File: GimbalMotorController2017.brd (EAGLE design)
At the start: 112.4 x 80 mm, 143 parts, among them J3 APP_2POS_CONFIG5V_HORIZ, Q1 MOSFET-NCHANNELFQP30N06L, Q2 MOSFET-NCHANNELFQP30N06L, Q3 MOSFET-NCHANNELFQP30N06L, Q4 MOSFET-NCHANNELFQP30N06L, Q5 MOSFET-NCHANNELFQP30N06L, Q6 MOSFET-NCHANNELFQP30N06L, Q7 MOSFET-PCHANNEL, Q8 MOSFET-PCHANNEL, Q9 MOSFET-NCHANNELAO3404A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

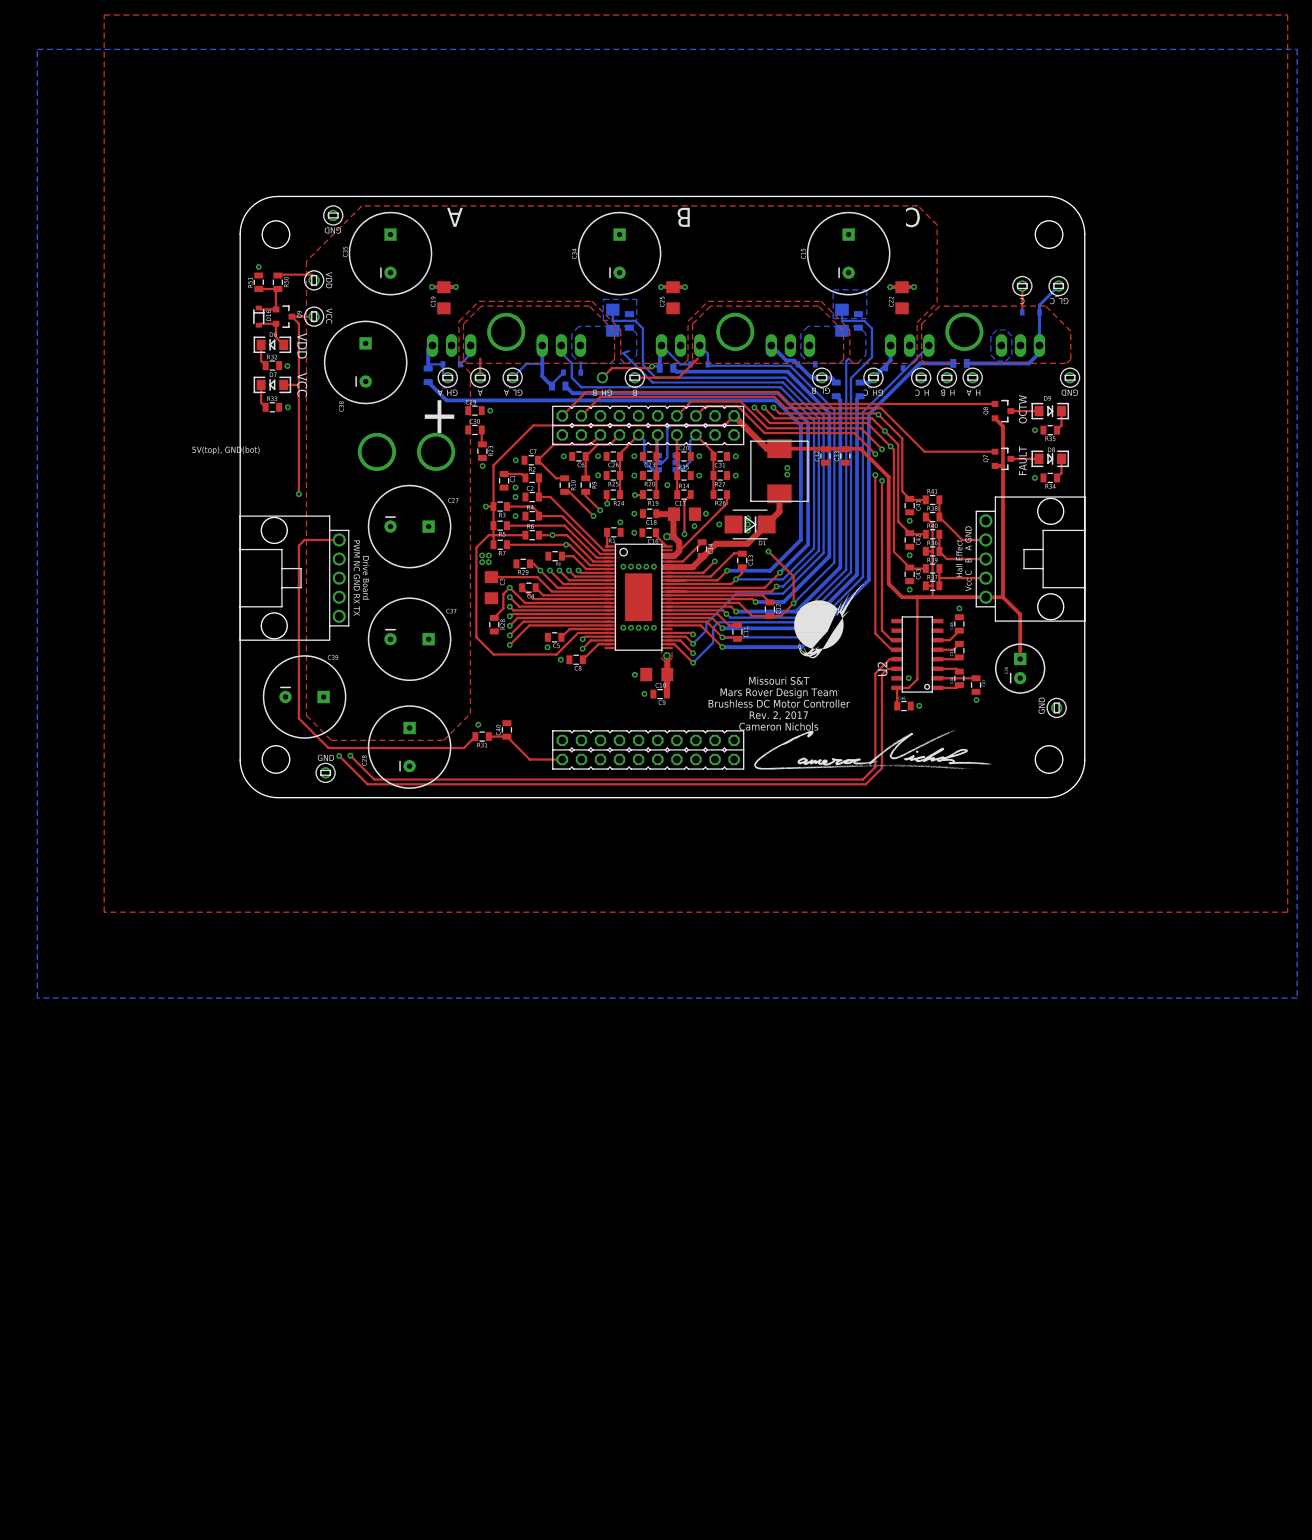
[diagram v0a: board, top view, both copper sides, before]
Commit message: changed power filtering cap count and R26 value for 12v to 3.3v conversion
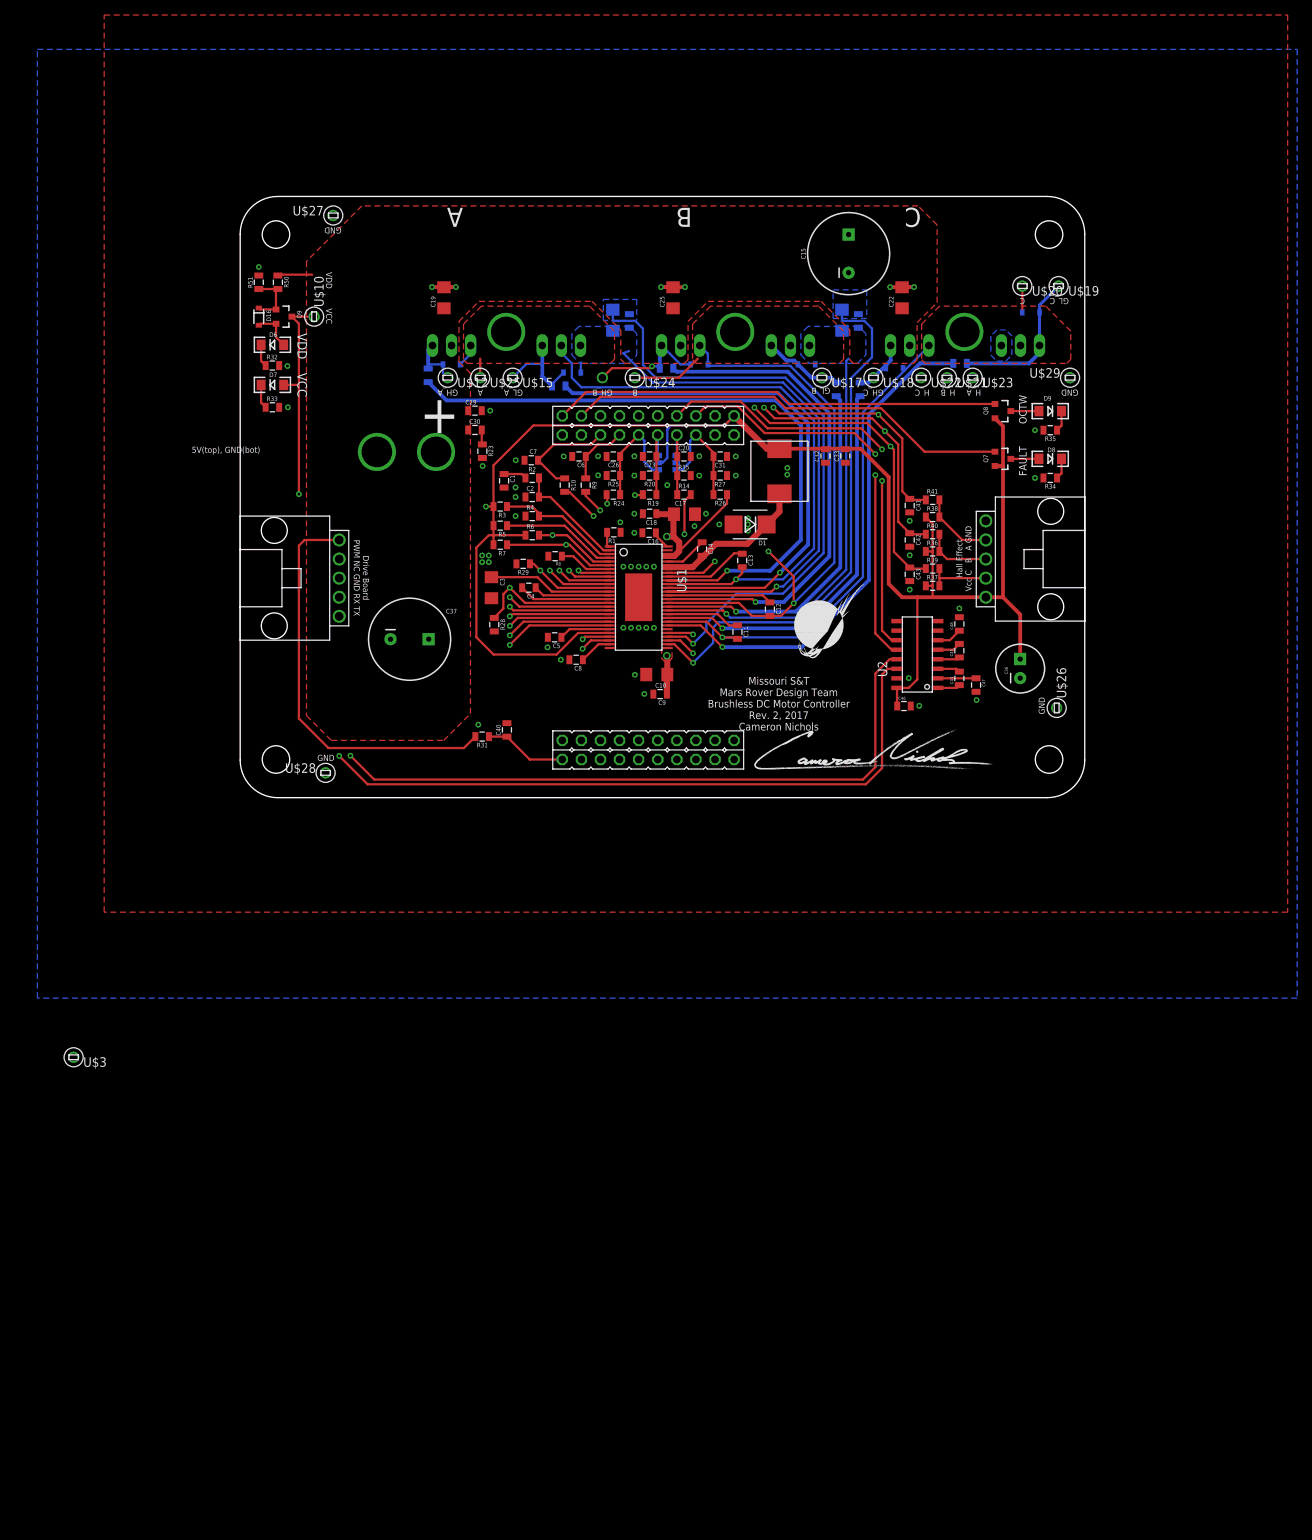
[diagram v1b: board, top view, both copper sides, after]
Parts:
- removed C27, C28, C34, C35, C38, C39: 220u, SparkFun-Passives:CPOL-RADIAL-1000UF-25V
- removed U$11: TEST_POINT_0.1INDIAM, MRDT-Connectors:TEST_POINT_0.1INDIAM
- added U$3: TEST_POINT_0.1INDIAM, MRDT-Connectors:TEST_POINT_0.1INDIAM
- R26: value 46.4k -> 13.2k
- U$1: device DRV8301:DCA -> MRDT-ICs:TFSOP-56
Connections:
- new net N$36: C15.1
- new net N$37: U$3.P$1
- net GND: no longer C27.2, C28.2, C34.2, C35.2, C38.2, C39.2
- net PVDD: no longer C15.1, C27.1, C28.1, C34.1, C35.1, C38.1, C39.1, U$11.P$1

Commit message: added CSD18533Q5A fets to Phase C in place of previously used fets
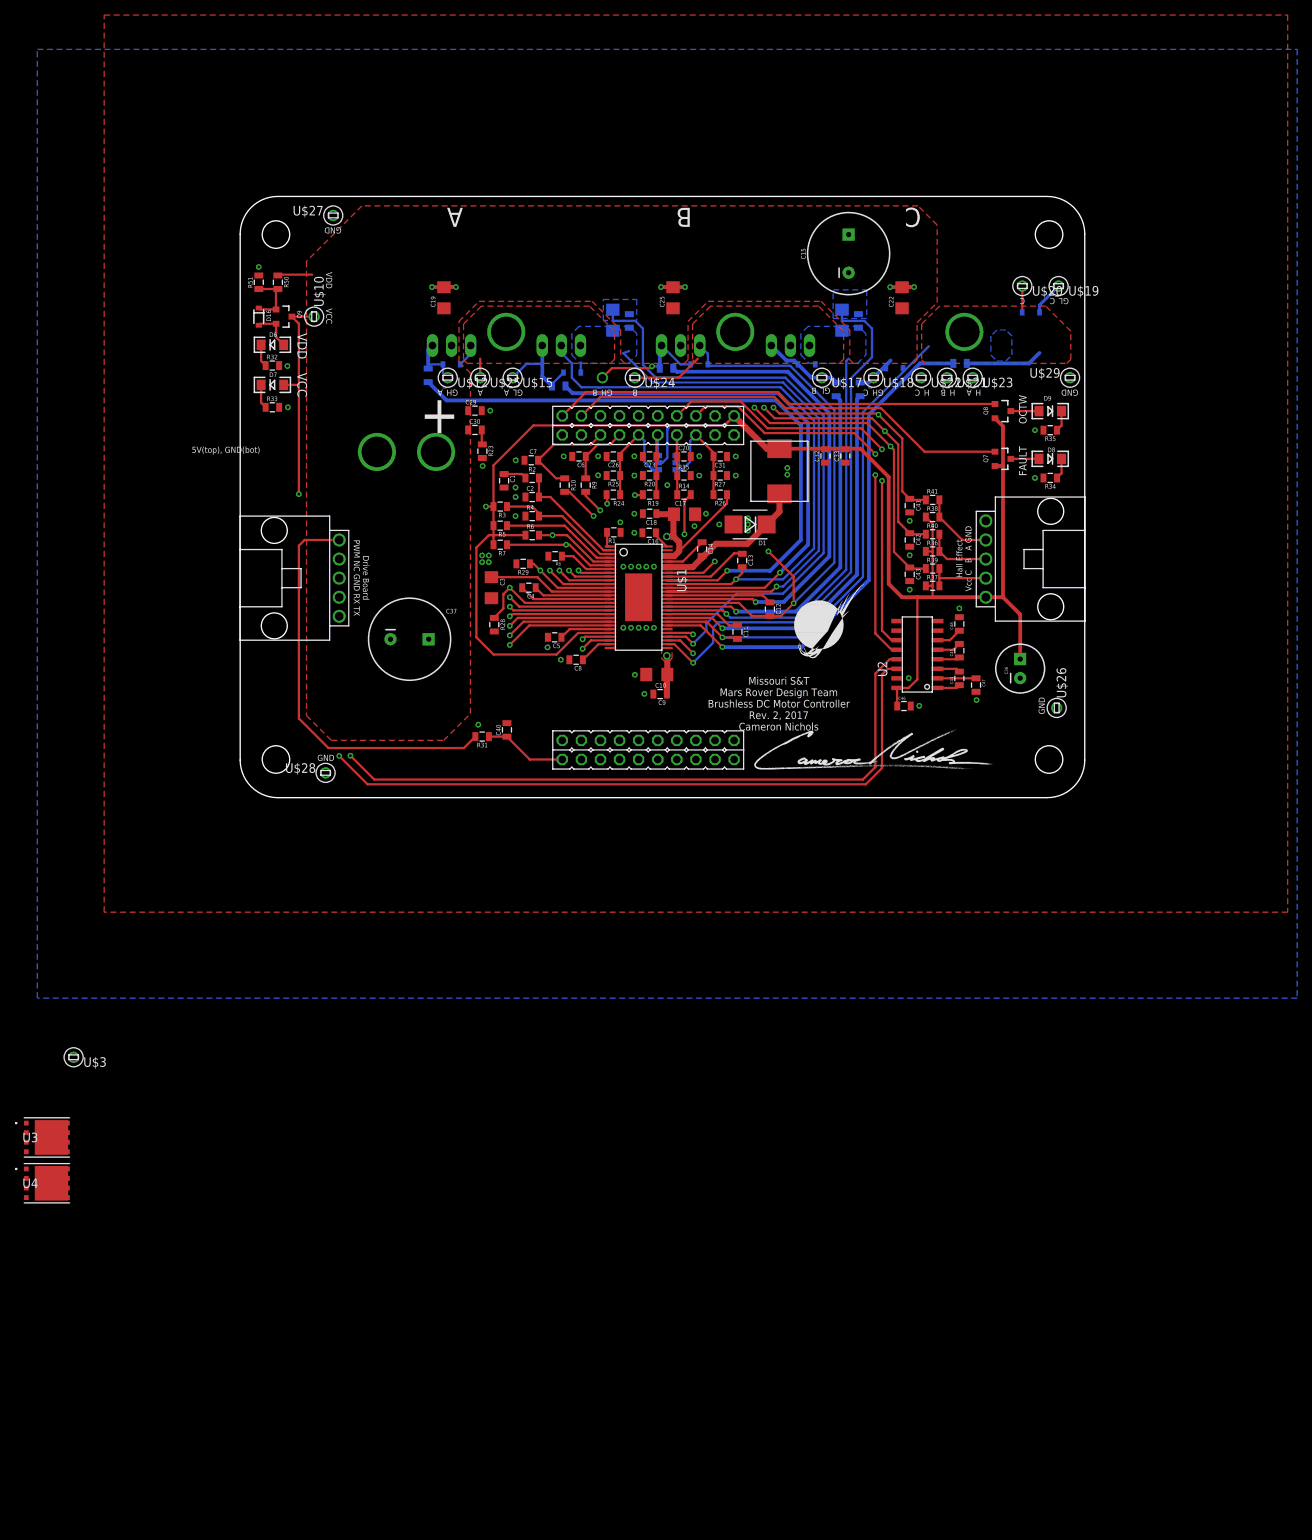
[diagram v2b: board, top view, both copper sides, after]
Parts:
- removed Q5, Q6: MOSFET-NCHANNELFQP30N06L, SparkFun-DiscreteSemi:TO220V
- added U3, U4: CSD18533Q5A, CSD18533:DQJ8
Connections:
- net GND: now also U4.3; no longer Q6.3
- net N$17: now also U3.4; no longer Q5.1
- net N$18: now also U4.4; no longer Q6.1
- net PVDD: now also U3.8; no longer Q5.2
- net SH_C: now also U3.3, U4.8; no longer Q5.3, Q6.2
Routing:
- net N$18: track 20.2 -> 14.8 mm
- net N$17: track 7.59 -> 5.59 mm
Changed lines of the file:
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@@
 <attribute name="PROD_ID" value="TRANS-10060" x="70.993" y="58.89625" size="1.778" layer="28" rot="MR180" display="off"/>
-</element>
-<element name="Q5" library="SparkFun-DiscreteSemi" package="TO220V" value="MOSFET-NCHANNELFQP30N06L" x="86.868" y="58.89625" smashed="yes" rot="MR180">
-<attribute name="NAME" x="90.424" y="55.46725" size="0.6096" layer="26" ratio="10" rot="MR180"/>
-<attribute name="PROD_ID" value="TRANS-10060" x="86.868" y="58.89625" size="1.778" layer="28" rot="MR180" display="off"/>
-</element>
-<element name="Q6" library="SparkFun-DiscreteSemi" package="TO220V" value="MOSFET-NCHANNELFQP30N06L" x="101.6" y="58.89625" smashed="yes" rot="MR0">
-<attribute name="NAME" x="98.171" y="61.05525" size="0.6096" layer="26" ratio="10" rot="MR0"/>
-<attribute name="PROD_ID" value="TRANS-10060" x="101.6" y="58.89625" size="1.778" layer="28" rot="MR0" display="off"/>
 </element>
 <element name="Q7" library="SparkFun-DiscreteSemi" package="SOT23-3" value="MOSFET-PCHANNEL" x="99.21875" y="43.815" smashed="yes" rot="R270">
@@
 <element name="C48" library="SparkFun-Passives" package="0805" value="0.1u" x="93.472" y="21.844" rot="R90"/>
 <element name="U$3" library="MRDT-Connectors" package="TEST_POINT_0.1INDIAM" value="TEST_POINT_0.1INDIAM" x="-24.384" y="-35.814"/>
+<element name="U3" library="CSD18533" package="DQJ8" value="CSD18533Q5A" x="-27.94" y="-46.482">
+<attribute name="MANUFACTURER_PART_NUMBER" value="CSD18533Q5A" x="-27.94" y="-46.482" size="1.778" layer="27" display="off"/>
+<attribute name="VENDOR" value="Texas Instruments" x="-27.94" y="-46.482" size="1.778" layer="27" display="off"/>
+</element>
+<element name="U4" library="CSD18533" package="DQJ8" value="CSD18533Q5A" x="-27.94" y="-52.578">
+<attribute name="MANUFACTURER_PART_NUMBER" value="CSD18533Q5A" x="-27.94" y="-52.578" size="1.778" layer="27" display="off"/>
+<attribute name="VENDOR" value="Texas Instruments" x="-27.94" y="-52.578" size="1.778" layer="27" display="off"/>
+</element>
 </elements>
 <signals>
@@
 </polygon>
 <contactref element="U$8" pad="5"/>
-<contactref element="Q6" pad="3"/>
 <polygon width="0.508" layer="16" thermals="no">
 <vertex x="97.663" y="60.16625"/>
@@
 <vertex x="-24.892" y="-19.558"/>
 </polygon>
-<wire x1="99.06" y1="58.89625" x2="101.847" y2="63.3095" width="0" layer="19" extent="16-16"/>
-<wire x1="108.204" y1="54.61" x2="99.06" y2="58.89625" width="0" layer="19" extent="1-1"/>
+<contactref element="U4" pad="3"/>
+<wire x1="108.204" y1="54.61" x2="101.847" y2="63.3095" width="0" layer="19" extent="16-16"/>
 <wire x1="104.66875" y1="47.625" x2="108.204" y2="54.61" width="0" layer="19" extent="1-1"/>
 <wire x1="103.53675" y1="47.625" x2="104.66875" y2="47.625" width="0" layer="19" extent="1-1"/>
@@
 <wire x1="17.78" y1="19.812" x2="31.59125" y2="20.84875" width="0" layer="19" extent="1-1"/>
 <wire x1="10.95375" y1="27.94" x2="17.78" y2="19.812" width="0" layer="19" extent="1-1"/>
-<wire x1="87.4395" y1="66.675" x2="99.06" y2="58.89625" width="0" layer="19" extent="1-1"/>
-<wire x1="80.04175" y1="63.0665" x2="84.2645" y2="66.675" width="0" layer="19" extent="16-16"/>
-<wire x1="77.851" y1="63.66175" x2="80.04175" y2="63.0665" width="0" layer="19" extent="16-16"/>
-<wire x1="78.74" y1="68.58" x2="77.851" y2="63.66175" width="0" layer="19" extent="16-16"/>
 <wire x1="15.97025" y1="44.73575" x2="30.00375" y2="43.931" width="0" layer="19" extent="1-1"/>
 <wire x1="4.1275" y1="50.673" x2="15.97025" y2="44.73575" width="0" layer="19" extent="1-1"/>
@@
 <wire x1="0.254" y1="69.342" x2="0.254" y2="68.21" width="0" layer="19" extent="1-1"/>
 <wire x1="10.16" y1="76.2" x2="0.254" y2="69.342" width="0" layer="19" extent="1-1"/>
+<wire x1="87.4395" y1="66.675" x2="101.847" y2="63.3095" width="0" layer="19" extent="16-16"/>
+<wire x1="80.04175" y1="63.0665" x2="84.2645" y2="66.675" width="0" layer="19" extent="16-16"/>
+<wire x1="77.851" y1="63.66175" x2="80.04175" y2="63.0665" width="0" layer="19" extent="16-16"/>
+<wire x1="78.74" y1="68.58" x2="77.851" y2="63.66175" width="0" layer="19" extent="16-16"/>
 <wire x1="23.3045" y1="66.675" x2="10.16" y2="76.2" width="0" layer="19" extent="1-1"/>
 <wire x1="47.371" y1="62.47765" x2="46.5345" y2="44.1325" width="0" layer="19" extent="1-16"/>
@@
 <wire x1="53.7845" y1="66.675" x2="49.56175" y2="63.0665" width="0" layer="19" extent="16-16"/>
 <wire x1="9.144" y1="2.032" x2="17.78" y2="19.812" width="0" layer="19" extent="1-1"/>
+<wire x1="-30.675071875" y1="-53.213" x2="9.144" y2="2.032" width="0" layer="19" extent="1-1"/>
 </signal>
 <signal name="N$3">
@@
 <contactref element="Q3" pad="2"/>
 <contactref element="C22" pad="1"/>
-<contactref element="Q5" pad="2"/>
 <contactref element="C25" pad="1"/>
 <contactref element="C29" pad="1"/>
@@
 </polygon>
 <contactref element="C37" pad="1"/>
-<wire x1="86.868" y1="58.89625" x2="85.852" y2="63.84625" width="0" layer="19" extent="1-1"/>
+<contactref element="U3" pad="8"/>
 <wire x1="56.388" y1="58.89625" x2="85.852" y2="63.84625" width="0" layer="19" extent="1-1"/>
 <wire x1="55.372" y1="63.84625" x2="56.388" y2="58.89625" width="0" layer="19" extent="1-1"/>
@@
 <wire x1="7.366" y1="68.326" x2="24.892" y2="63.84625" width="0" layer="19" extent="1-1"/>
 <wire x1="22.86" y1="19.812" x2="23.84425" y2="44.73575" width="0" layer="19" extent="1-1"/>
+<wire x1="-25.204928125" y1="-44.577" x2="22.86" y2="19.812" width="0" layer="19" extent="1-1"/>
 </signal>
 <signal name="GL_C">
@@
 <contactref element="U$1" pad="36"/>
 <contactref element="C11" pad="2"/>
-<contactref element="Q5" pad="3"/>
-<contactref element="Q6" pad="2"/>
 <contactref element="R24" pad="1"/>
 <contactref element="U$7" pad="P$1"/>
@@
 <wire x1="80.645" y1="50.031" x2="86.2365" y2="55.6225" width="0.3048" layer="16"/>
 <wire x1="86.2365" y1="55.6225" x2="89.408" y2="58.794" width="0.3048" layer="16"/>
-<wire x1="89.408" y1="58.794" x2="89.408" y2="58.89625" width="0.3048" layer="16"/>
 <wire x1="85.986" y1="55.88" x2="85.986" y2="55.873" width="0.3048" layer="16"/>
 <wire x1="85.986" y1="55.873" x2="86.2365" y2="55.6225" width="0.3048" layer="16"/>
+<contactref element="U3" pad="3"/>
+<contactref element="U4" pad="8"/>
+<wire x1="94.13875" y1="60.706" x2="101.854" y2="63.754" width="0" layer="19" extent="1-1"/>
+<wire x1="89.408" y1="58.794" x2="94.13875" y2="60.706" width="0" layer="19" extent="16-16"/>
+<wire x1="-25.204928125" y1="-50.673" x2="55.88" y2="17.272" width="0" layer="19" extent="1-15"/>
+<wire x1="-30.675071875" y1="-47.117" x2="-25.204928125" y2="-50.673" width="0" layer="19" extent="1-1"/>
 </signal>
 <signal name="GH_C">
@@
 </signal>
 <signal name="N$17">
-<contactref element="Q5" pad="1"/>
 <contactref element="R21" pad="1"/>
 <contactref element="D14" pad="C"/>
@@
 <wire x1="82.042" y1="54.61" x2="83.566" y2="56.134" width="0.508" layer="16"/>
 <wire x1="83.566" y1="56.134" x2="84.328" y2="56.896" width="0.508" layer="16"/>
-<wire x1="84.328" y1="56.896" x2="84.328" y2="58.89625" width="0.508" layer="16"/>
 <wire x1="83.686" y1="55.88" x2="83.566" y2="56" width="0.4064" layer="16"/>
 <wire x1="83.566" y1="56" x2="83.566" y2="56.134" width="0.4064" layer="16"/>
+<contactref element="U3" pad="4"/>
+<wire x1="-30.675071875" y1="-48.387" x2="80.264" y2="53.95425" width="0" layer="19" extent="1-16"/>
 </signal>
 <signal name="N$18">
-<contactref element="Q6" pad="1"/>
 <contactref element="R22" pad="1"/>
 <contactref element="D15" pad="C"/>
@@
 <wire x1="104.147" y1="64.269" x2="106.68" y2="66.802" width="0.4064" layer="16"/>
 <wire x1="102.743" y1="56.515" x2="104.14" y2="57.912" width="0.508" layer="16"/>
-<wire x1="104.14" y1="57.912" x2="104.14" y2="58.89625" width="0.508" layer="16"/>
-<wire x1="104.14" y1="58.89625" x2="104.14" y2="63.3025" width="0.4064" layer="16"/>
 <wire x1="104.14" y1="63.3025" x2="104.147" y2="63.3095" width="0.4064" layer="16"/>
+<contactref element="U4" pad="4"/>
+<wire x1="104.14" y1="57.912" x2="104.147" y2="63.3095" width="0" layer="19" extent="16-16"/>
+<wire x1="-30.675071875" y1="-54.483" x2="94.46725" y2="56.515" width="0" layer="19" extent="1-16"/>
 </signal>
 <signal name="BSENSE">
